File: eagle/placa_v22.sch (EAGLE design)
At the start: 32 parts, among them IC1 7805, Q1 IRF740, Y1 16MHz

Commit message: Eletronica
git-svn-id: https://mbs-bot.googlecode.com/svn/trunk@214 3c29fe3e-da84-11de-ae71-c59d11f48c9c
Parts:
- removed JP1: AVR-ISP-6VERT, avr-7:AVR-ISP-6VERT
- removed R7: 1k, SparkFun:RESISTORKIT
- added C14, C9: 100n, SparkFun:CAPPTH1
- added D1: (no value), SparkFun:DIODEPTH
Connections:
- removed net D11: JP1.4, MCU.PB3(MOSI/OC2A/PCINT3)
- net +5V: no longer JP1.2
- net D12: no longer JP1.1
- net D13: no longer JP1.3
- net D9: now also Q1.G; no longer R7.1
- net GND: no longer JP1.6
- net N$10: now also C9.2; no longer JP1.5, MCU.PC6(/RESET/PCINT14), R3.2
- net N$11: now also C14.1, D1.A
- net N$2: now also C9.1, MCU.PC6(/RESET/PCINT14), R3.2; no longer Q1.G, R7.2
- net VCC: now also C14.2, D1.C
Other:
- moved on the sheet: ARMA-1, ARMA-2, C1, C2, LED1, Q1, R6, Y1

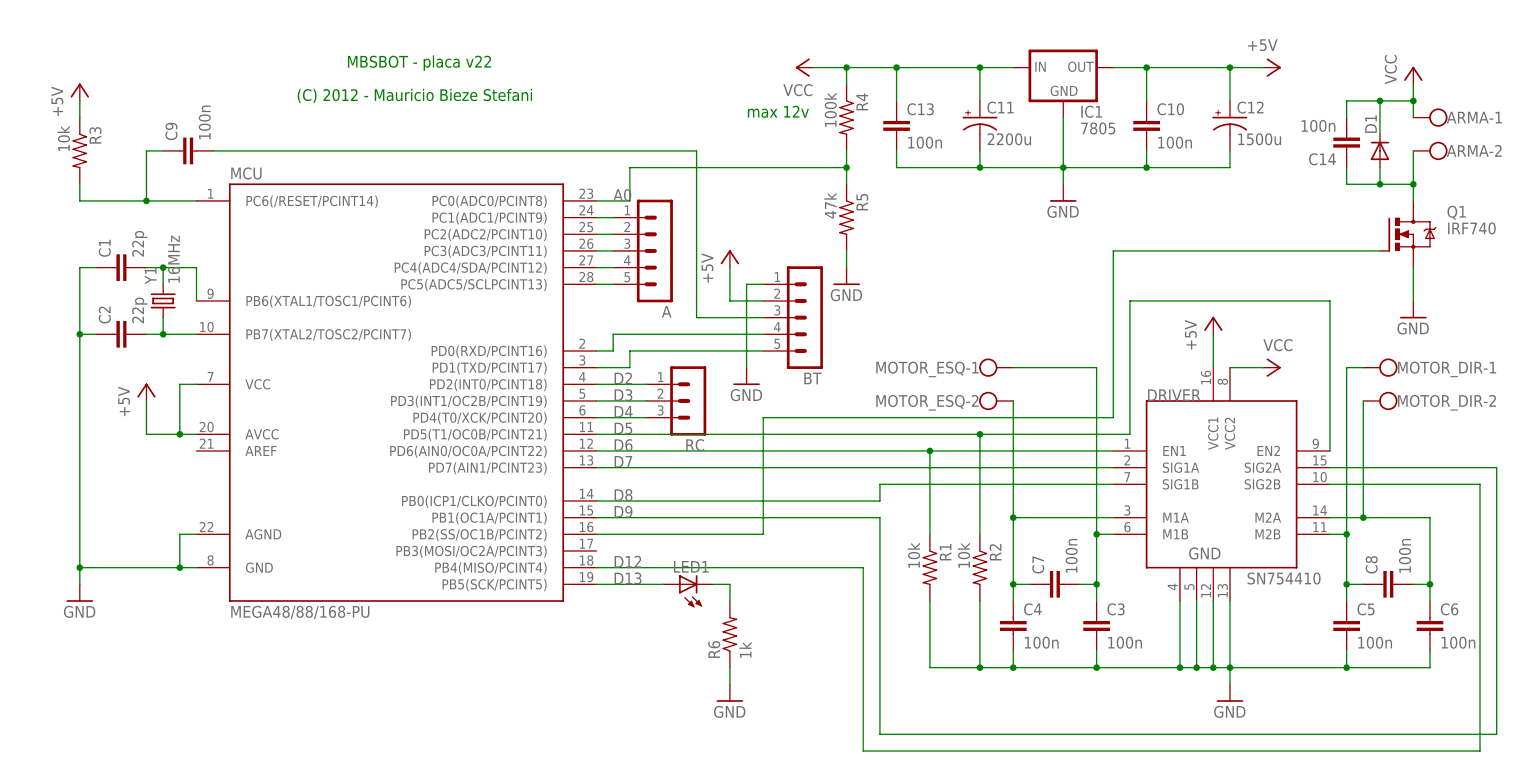
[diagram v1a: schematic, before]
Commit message: Nova classe ConfigSensor pra armazenar na EEPROM. Ajustes no circuito e placa.
git-svn-id: https://mbs-bot.googlecode.com/svn/trunk@216 3c29fe3e-da84-11de-ae71-c59d11f48c9c
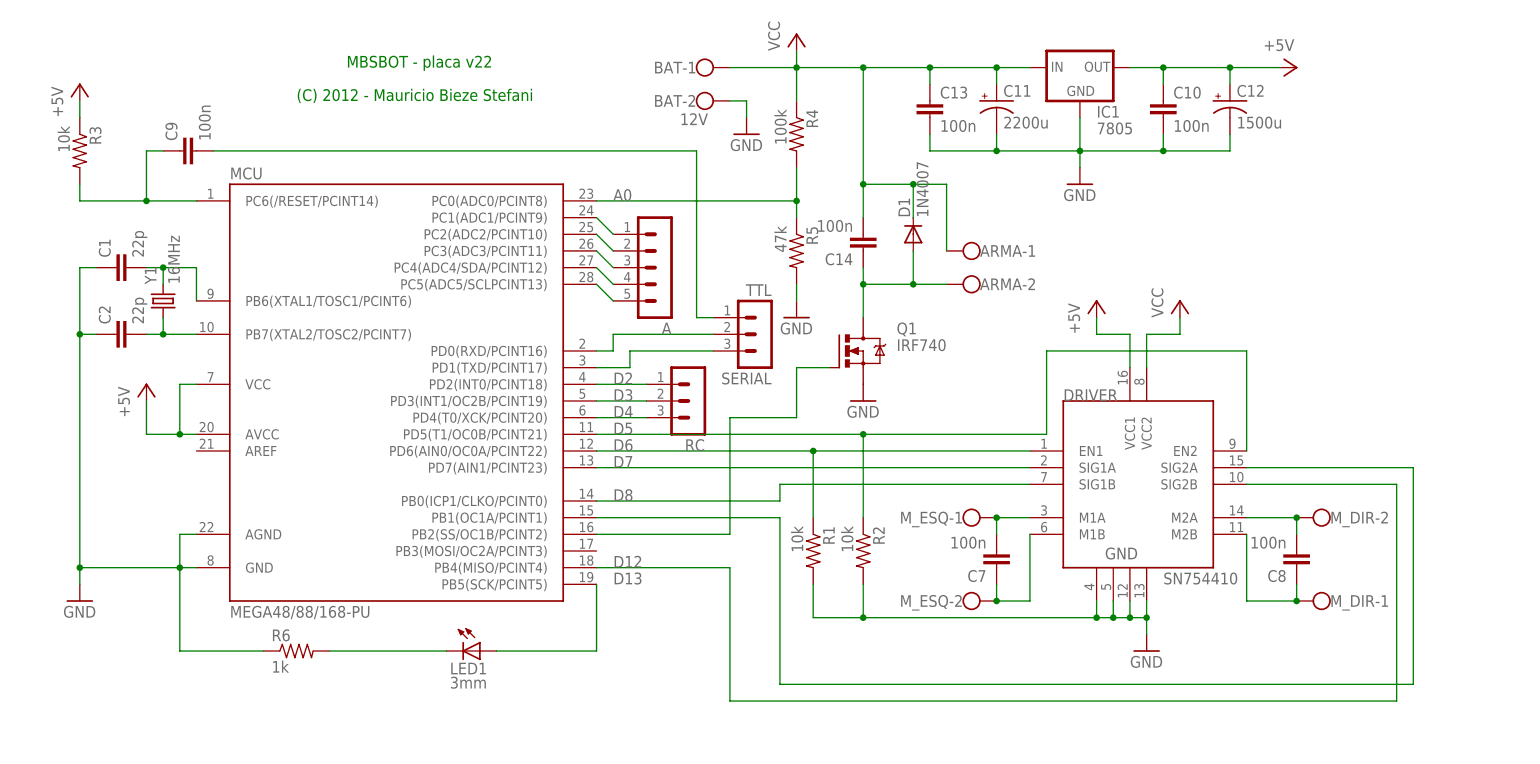
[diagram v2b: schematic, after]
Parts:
- removed BT: (no value), con-lstb:MA05-1
- removed C3, C4, C5, C6: 100n, SparkFun:CAPPTH1
- removed MOTOR_DIR, MOTOR_ESQ: (no value), con-wago-500:W237-102
- added BAT: 12V, con-wago-500:W237-102
- added M_DIR, M_ESQ: (no value), con-wago-500:W237-102
- added SERIAL: TTL, con-lstb:MA03-1
- D1: value (none) -> 1N4007
- LED1: value (none) -> 3mm
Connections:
- removed net D9: DRIVER.SIG2A, MCU.PB1(OC1A/PCINT1), MCU.PB2(SS/OC1B/PCINT2), Q1.G
- new net N$17: MCU.PB2(SS/OC1B/PCINT2), Q1.G
- new net N$19: DRIVER.SIG2A, MCU.PB1(OC1A/PCINT1)
- net +5V: no longer BT.2
- net A: now also SERIAL.2; no longer BT.4
- net GND: now also BAT-2.KL; no longer BT.1, C3.2, C4.2, C5.2, C6.2
- net N$10: now also SERIAL.1; no longer BT.3
- net N$5: now also C7.2, M_ESQ-1.KL; no longer C4.1, C7.1, MOTOR_ESQ-2.KL
- net N$6: now also C7.1, M_ESQ-2.KL; no longer C3.1, C7.2, MOTOR_ESQ-1.KL
- net N$7: now also M_DIR-1.KL; no longer C5.1, MOTOR_DIR-1.KL
- net N$8: now also M_DIR-2.KL; no longer C6.1, MOTOR_DIR-2.KL
- net N$9: now also SERIAL.3; no longer BT.5
- net VCC: now also BAT-1.KL
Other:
- note removed: "max 12v"
- moved on the sheet: A, ARMA-1, ARMA-2, C10, C11, C12, C13, C14, C7, C8, D1, DRIVER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
